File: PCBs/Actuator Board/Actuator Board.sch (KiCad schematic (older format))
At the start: 20 parts

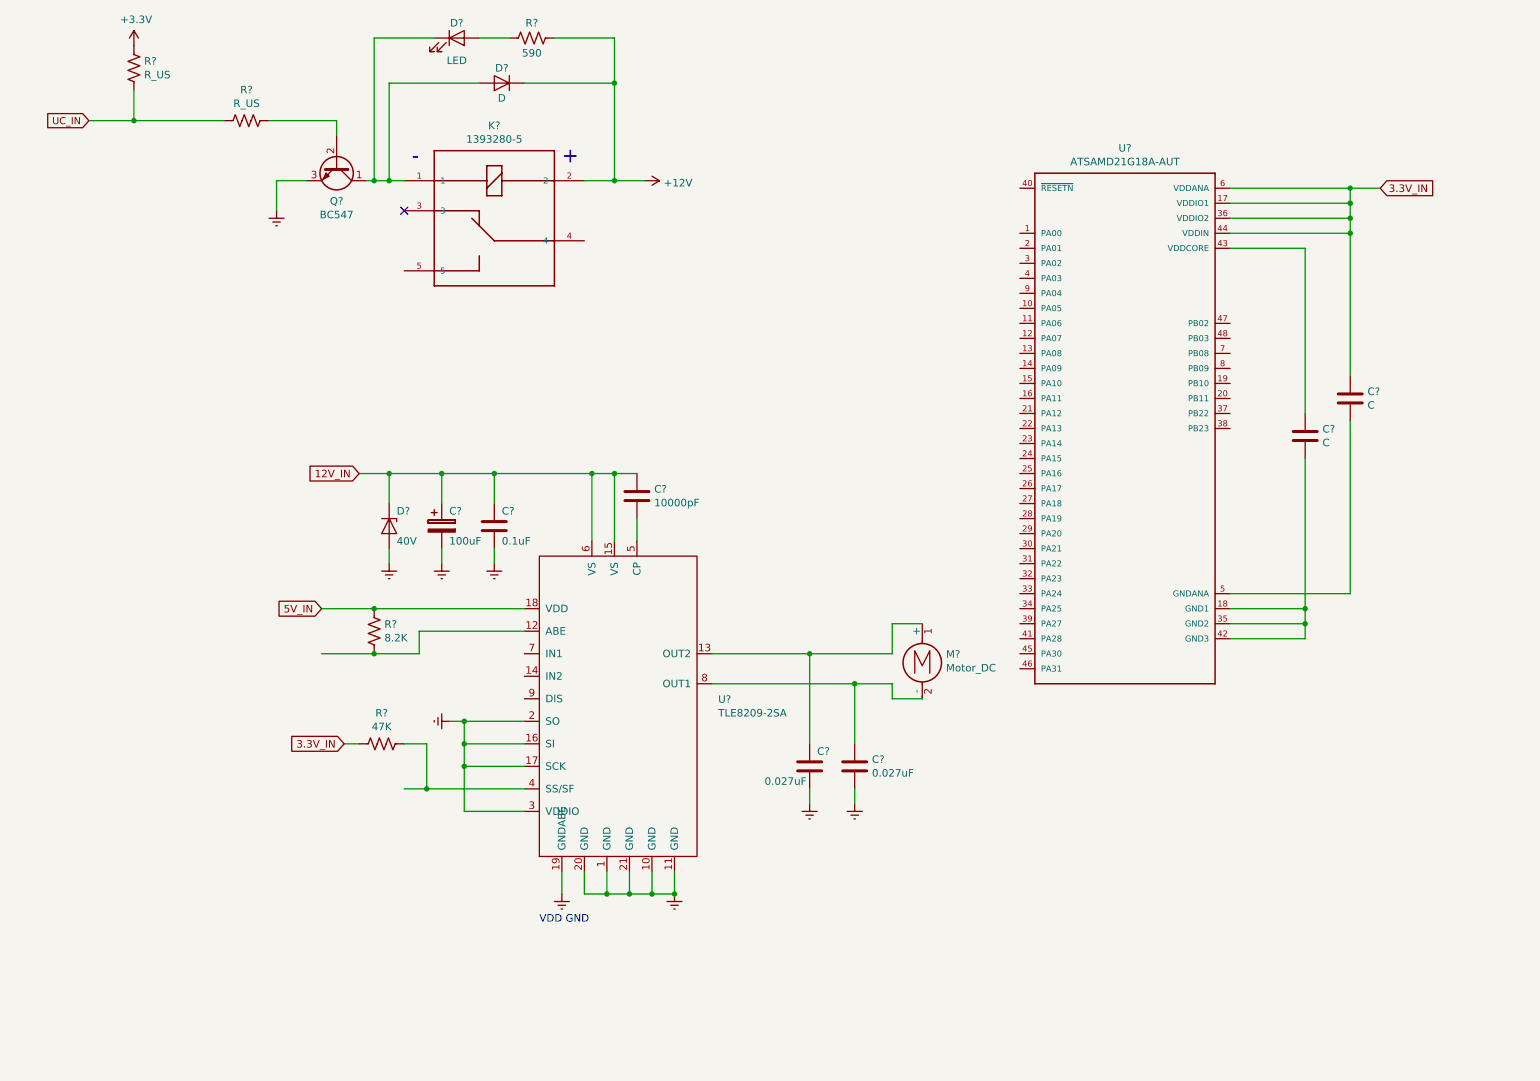
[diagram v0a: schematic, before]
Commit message: Filled in some information about  transistor
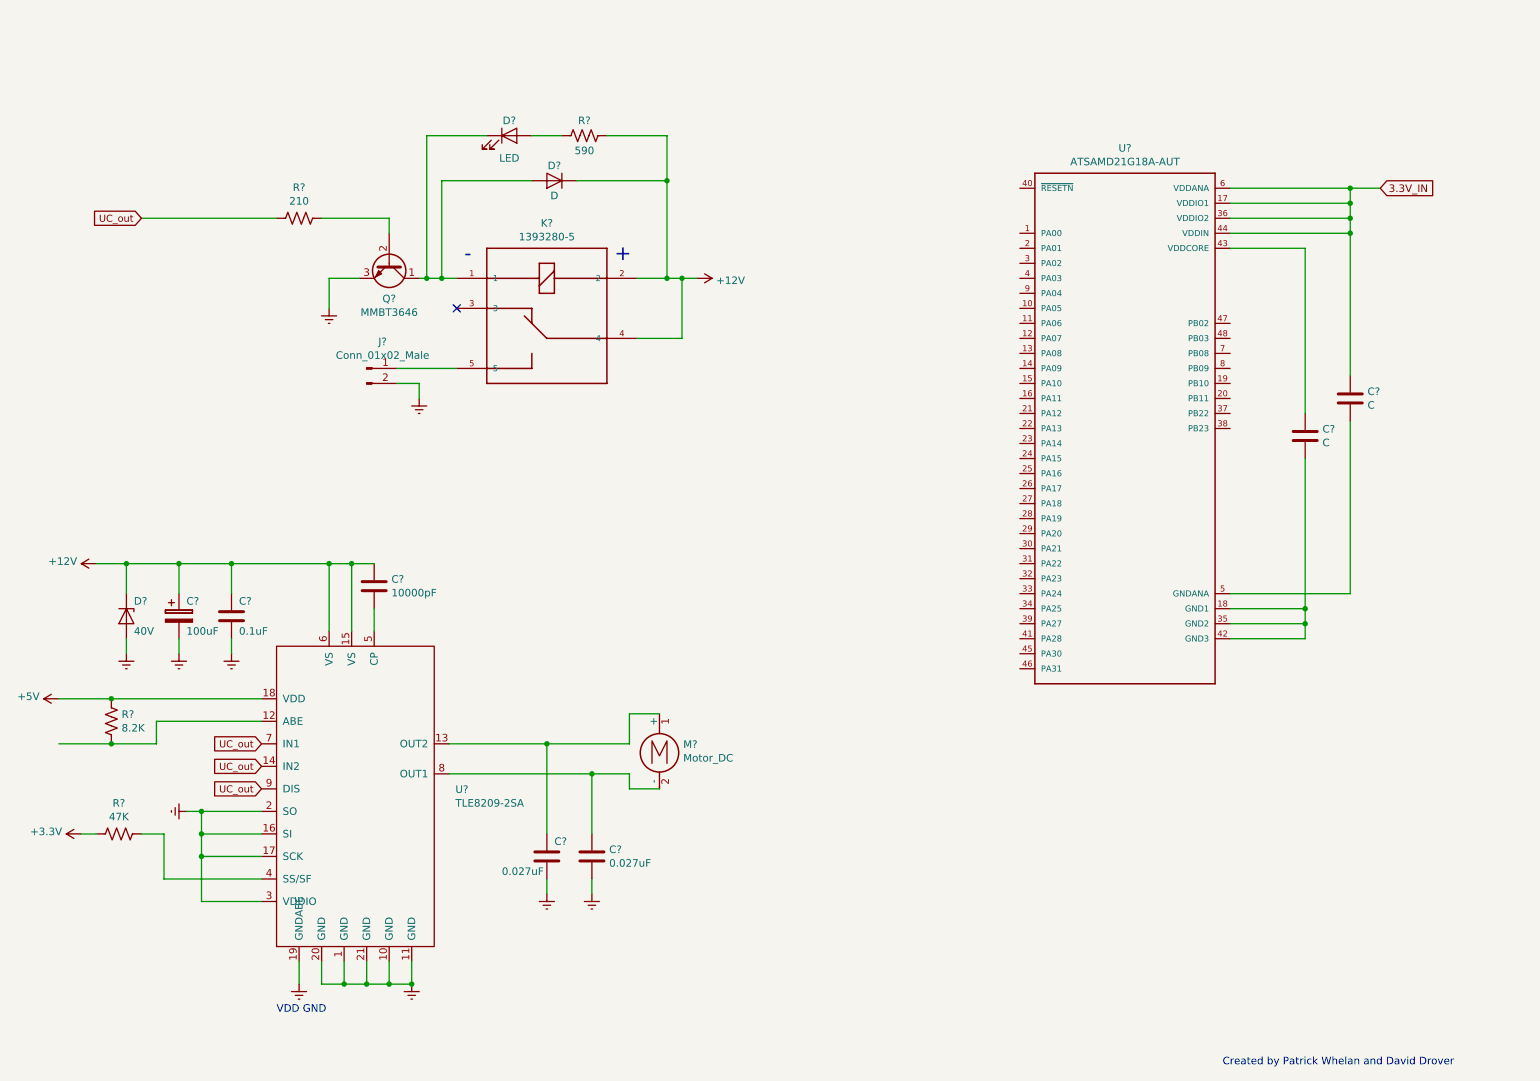
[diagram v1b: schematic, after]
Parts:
- removed R?: R_US, symbol Device:R_US
- added J?: Conn_01x02_Male, symbol Connector:Conn_01x02_Male
- Q?: value BC547 -> MMBT3646; footprint Package_TO_SOT_THT:TO-92_Inline -> (none)
- R?: value R_US -> 210
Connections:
- net 12V_IN is gone; now on net +12V: C?.1, C?.1, C?.1, D?.1 (K), U?.15 (VS), U?.6 (VS)
- net UC_IN is gone; now on net UC_out: R?.2
- net +12V: now also K?.4
- net +3V3: now also R?.2
- net 3.3V_IN: no longer R?.2
- net Earth: now also J?.2 (Pin_2)
- net at K?.5: now also J?.1 (Pin_1)
- net UC_out: now reaches U?.14 (IN2)
- net UC_out: now also U?.7 (IN1), U?.9 (DIS)
- net 5V_IN renamed +5V
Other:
- note added: "Created by Patrick Whelan and David Drover"
- moved on the sheet: C?, D?, K?, M?, Q?, R?

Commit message: Finished Main Controller
Copied over Mark's main controller design
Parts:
- removed C? (x2): C, symbol Device:C
- removed U?: ATSAMD21G18A-AUT, QFP50P900X900X120-48N, symbol ATSAMD21G18A-AUT:ATSAMD21G18A-AUT
- added C?: 0.1uF, symbol Device:C
- added C? (x2): 22pF, symbol Device:C
- added D?: LED, symbol Device:LED
- added R?: 680, symbol Device:R_US
- added R?: 10k, symbol Device:R_US
- added SW?: SW_Push, symbol Switch:SW_Push
- added U?: ATSAMD21E16L-MFT, digikey-footprints:TQFP-48_7x7mm, symbol EER:ATSAMD21E16L-MFT
- added Y?: 32.7680kHz, symbol Device:Crystal
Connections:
- net +3V3: now also D?.2 (A), R?.2, U?.30 (VDDIN)
- net Earth: now also C?.2, C?.2, C?.2, SW?.1, U?.10 (GND), U?.28 (GND)
- net UC_out: no longer U?.14 (IN2), U?.7 (IN1), U?.9 (DIS)
- net UC_OUT: now reaches R?.1, U?.4 (SS/SF)
- net UC_OUT: now also U?.14 (IN2), U?.7 (IN1), U?.9 (DIS)
- new net: C?.1, U?.1 (PA00), Y?.1
- new net: R?.1, U?.14 (PA11)
- new net: C?.1, U?.2 (PA01), Y?.2
- new net: C?.1, U?.29 (VDDCORE)
- new net: D?.1 (K), R?.2
- new net 3V3_FILT: U?.9 (VDD/ANA)
- new net SCL: U?.22 (PA23)
- new net SDA: U?.21 (PA22)
- new net SWCLK: U?.31 (PA30)
- new net SWDIO: U?.32 (PA31)
- new net USB+: U?.24 (PA25)
- new net USB-: U?.23 (PA24)
- new net VIOUT1: U?.6 (PA05)
- new net VIOUT2: U?.7 (PA06)
- new net VIOUT3: U?.8 (PA07)
- new net ~RESET~: R?.1, SW?.2, U?.26 (~RESET)
- no-connect marks 1 -> 15
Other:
- note added: "AIN5"
- note added: "AIN6"
- note added: "AIN7"
- note added: "TESTIO"
